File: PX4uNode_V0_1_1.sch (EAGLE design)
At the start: 129 parts, among them M3_MOUNT1101 MOUNT-HOLE3.1MM, M3_MOUNT1102 MOUNT-HOLE3.1MM, M3_MOUNT1103 MOUNT-HOLE3.1MM, M3_MOUNT1104 MOUNT-HOLE3.1MM, U101 STM32F4X7VX, U401 MAX3051, U402 MAX3051, X101 3.2x2.5 mm / 24 MHz / 15 ppm

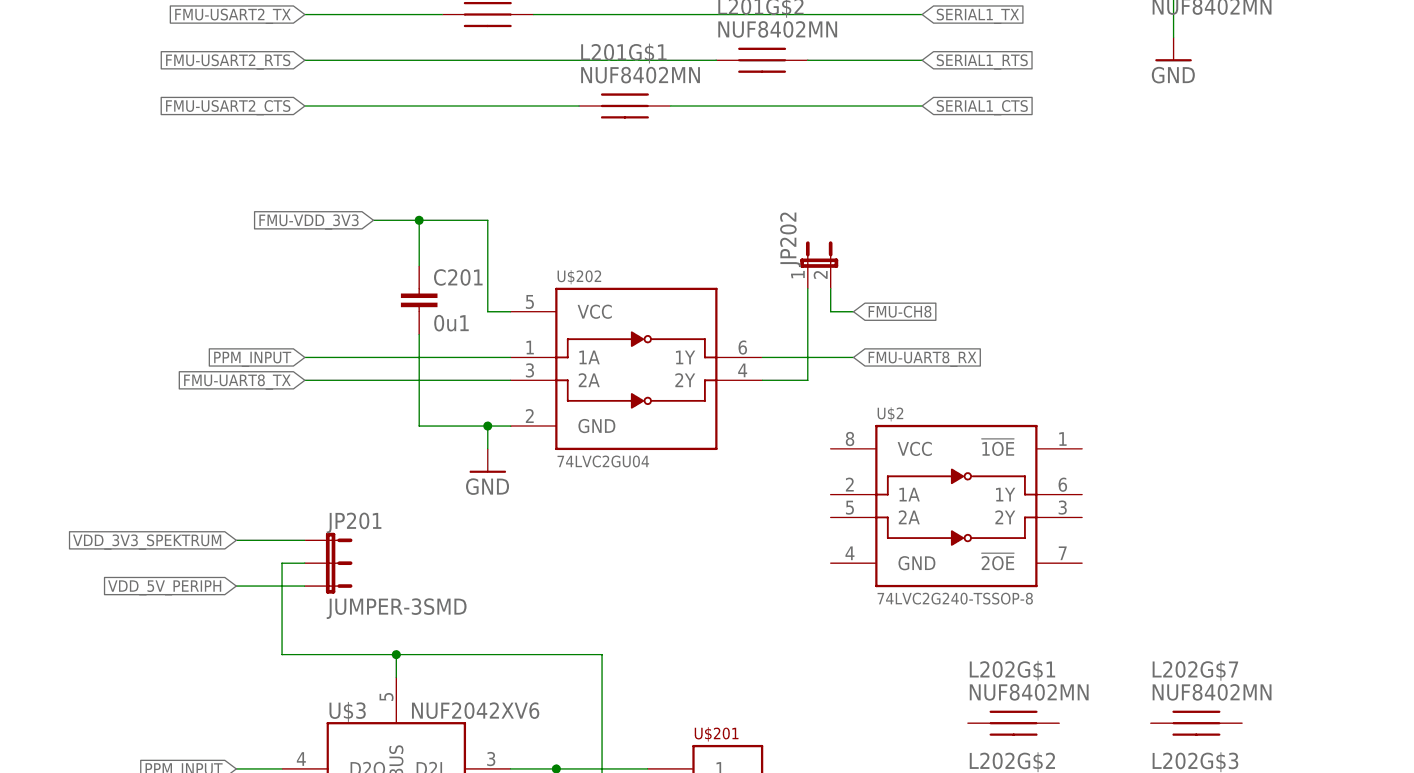
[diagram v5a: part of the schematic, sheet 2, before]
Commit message: Changed SBUS inverter for TSSOP part with output enable
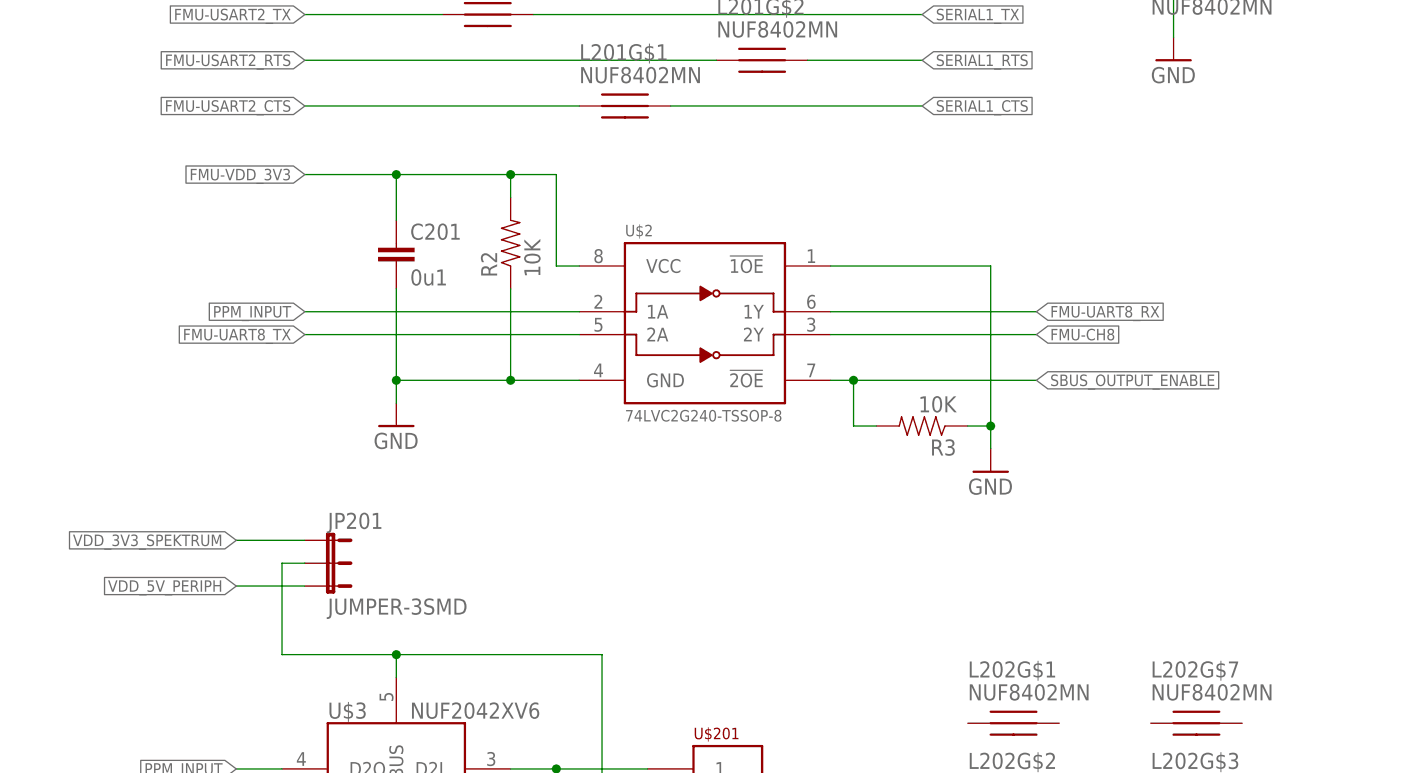
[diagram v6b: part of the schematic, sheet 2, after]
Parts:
- removed JP202: (no value), SparkFun-Passives:JUMPER-2SMD-NO
- removed U$202: 74LVC2GU04, pixhawk2:74LVC2GU04
- added R2, R3: 10K, pixhawk2:RESISTOR0402-RES
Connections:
- removed net !EX_VDD_5V_VALID: U101PORTB_L.PB5
- removed net N$5: JP202.1, U$202.2Y
- new net SBUS_OUTPUT_ENABLE: R3.2, U$2.!2OE, U101PORTB_L.PB5
- net FMU-CH8: now also U$2.2Y; no longer JP202.2
- net FMU-UART8_RX: now also U$2.1Y; no longer U$202.1Y
- net FMU-UART8_TX: now also U$2.2A; no longer U$202.2A
- net FMU-VDD_3V3: now also R2.2, U$2.VCC; no longer U$202.VCC
- net GND: now also R2.1, R3.1, U$2.!1OE, U$2.GND; no longer U$202.GND
- net PPM_INPUT: now also U$2.1A; no longer U$202.1A
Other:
- moved on the sheet: C201, U$2
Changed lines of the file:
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@@
 <attribute name="PARTNO" value="CC0402ZRY5V7BB104"/>
-</part>
-<part name="U$202" library="pixhawk2" deviceset="74LVC2GU04" device="">
-<attribute name="PARTNO" value="74LVC2GU04"/>
 </part>
 <part name="GND2" library="pixhawk2" deviceset="GND" device=""/>
@@
 <attribute name="BOM" value="EXCLUDE"/>
 <attribute name="PARTNO" value="*"/>
-</part>
-<part name="JP202" library="SparkFun-Passives" deviceset="JUMPER-2" device="SMD-NO">
-<attribute name="BOM" value="EXCLUDE"/>
 </part>
 <part name="JP1001" library="SparkFun-Connectors" deviceset="M01" device="SMD-4.5X1.5">
@@
 <part name="JP4" library="SparkFun-Connectors" deviceset="M01" device="PTH"/>
 <part name="U$2" library="pixhawk2" deviceset="74LVC2G240" device="-TSSOP-8"/>
+<part name="GND22" library="pixhawk2" deviceset="GND" device=""/>
+<part name="R2" library="pixhawk2" deviceset="RESISTOR" device="0402-RES" value="10K">
+<attribute name="PARTNO" value="RC0402FR-0710KL"/>
+</part>
+<part name="R3" library="pixhawk2" deviceset="RESISTOR" device="0402-RES" value="10K">
+<attribute name="PARTNO" value="RC0402FR-0710KL"/>
+</part>
 </parts>
 <sheets>
@@
 </segment>
 </net>
-<net name="!EX_VDD_5V_VALID" class="0">
+<net name="SBUS_OUTPUT_ENABLE" class="0">
 <segment>
 <pinref part="U101" gate="PORTB_L" pin="PB5"/>
-<wire x1="33.02" y1="96.52" x2="58.42" y2="96.52" width="0.1524" layer="91"/>
-<label x="58.42" y="96.52" size="1.27" layer="95" xref="yes"/>
+<wire x1="33.02" y1="96.52" x2="40.64" y2="96.52" width="0.1524" layer="91"/>
+<label x="40.64" y="96.52" size="1.27" layer="95" xref="yes"/>
 </segment>
 </net>
@@
 <instance part="L202" gate="G$7" x="147.32" y="60.96"/>
 <instance part="L202" gate="G$4" x="147.32" y="38.1"/>
-<instance part="U$202" gate="G$1" x="83.82" y="99.06">
-<attribute name="PARTNO" x="83.82" y="99.06" size="1.778" layer="96" display="off"/>
-</instance>
-<instance part="GND2" gate="1" x="68.58" y="88.9"/>
-<instance part="C201" gate="G$1" x="60.96" y="106.68">
-<attribute name="PARTNO" x="60.96" y="106.68" size="1.778" layer="96" display="off"/>
+<instance part="GND2" gate="1" x="58.42" y="93.98"/>
+<instance part="C201" gate="G$1" x="58.42" y="111.76" smashed="yes">
+<attribute name="PARTNO" x="58.42" y="111.76" size="1.778" layer="96" display="off"/>
+<attribute name="NAME" x="59.944" y="114.681" size="1.778" layer="95"/>
+<attribute name="VALUE" x="59.944" y="109.601" size="1.778" layer="96"/>
 </instance>
 <instance part="JP201" gate="G$1" x="50.8" y="81.28" rot="R270">
 <attribute name="BOM" x="50.8" y="81.28" size="1.778" layer="96" rot="R270" display="off"/>
-</instance>
-<instance part="JP202" gate="A" x="104.14" y="111.76">
-<attribute name="BOM" x="104.14" y="111.76" size="1.778" layer="96" display="off"/>
 </instance>
 <instance part="JP12" gate="G$1" x="220.98" y="147.32"/>
@@
 <instance part="GND19" gate="1" x="58.42" y="30.48"/>
 <instance part="U$3" gate="G$1" x="58.42" y="50.8"/>
-<instance part="U$2" gate="G$1" x="119.38" y="83.82"/>
+<instance part="U$2" gate="G$1" x="91.44" y="104.14"/>
+<instance part="GND22" gate="1" x="124.46" y="88.9"/>
+<instance part="R2" gate="G$1" x="71.12" y="114.3" rot="R90">
+<attribute name="PARTNO" x="71.12" y="114.3" size="1.778" layer="96" display="off"/>
+</instance>
+<instance part="R3" gate="G$1" x="116.84" y="93.98" rot="R180">
+<attribute name="PARTNO" x="116.84" y="93.98" size="1.778" layer="96" rot="R90" display="off"/>
+</instance>
 </instances>
 <busses>
@@
 <segment>
 <pinref part="GND2" gate="1" pin="GND"/>
-<wire x1="68.58" y1="91.44" x2="68.58" y2="93.98" width="0.1524" layer="91"/>
-<pinref part="U$202" gate="G$1" pin="GND"/>
-<wire x1="68.58" y1="93.98" x2="71.12" y2="93.98" width="0.1524" layer="91"/>
+<wire x1="58.42" y1="96.52" x2="58.42" y2="99.06" width="0.1524" layer="91"/>
+<wire x1="58.42" y1="99.06" x2="71.12" y2="99.06" width="0.1524" layer="91"/>
 <pinref part="C201" gate="G$1" pin="2"/>
-<wire x1="60.96" y1="104.14" x2="60.96" y2="93.98" width="0.1524" layer="91"/>
-<wire x1="60.96" y1="93.98" x2="68.58" y2="93.98" width="0.1524" layer="91"/>
-<junction x="68.58" y="93.98"/>
+<wire x1="71.12" y1="99.06" x2="78.74" y2="99.06" width="0.1524" layer="91"/>
+<wire x1="58.42" y1="109.22" x2="58.42" y2="99.06" width="0.1524" layer="91"/>
+<junction x="58.42" y="99.06"/>
+<pinref part="U$2" gate="G$1" pin="GND"/>
+<pinref part="R2" gate="G$1" pin="1"/>
+<wire x1="71.12" y1="109.22" x2="71.12" y2="99.06" width="0.1524" layer="91"/>
+<junction x="71.12" y="99.06"/>
 </segment>
 <segment>
@@
 <pinref part="U$3" gate="G$1" pin="GND"/>
 <wire x1="58.42" y1="33.02" x2="58.42" y2="35.56" width="0.1524" layer="91"/>
+</segment>
+<segment>
+<pinref part="GND22" gate="1" pin="GND"/>
+<wire x1="124.46" y1="91.44" x2="124.46" y2="93.98" width="0.1524" layer="91"/>
+<pinref part="U$2" gate="G$1" pin="!1OE"/>
+<wire x1="124.46" y1="93.98" x2="124.46" y2="111.76" width="0.1524" layer="91"/>
+<wire x1="124.46" y1="111.76" x2="106.68" y2="111.76" width="0.1524" layer="91"/>
+<pinref part="R3" gate="G$1" pin="1"/>
+<wire x1="121.92" y1="93.98" x2="124.46" y2="93.98" width="0.1524" layer="91"/>
+<junction x="124.46" y="93.98"/>
 </segment>
 </net>
@@
 </segment>
 <segment>
-<label x="48.26" y="101.6" size="1.27" layer="95" rot="R180" xref="yes"/>
-<pinref part="U$202" gate="G$1" pin="1A"/>
-<wire x1="48.26" y1="101.6" x2="71.12" y2="101.6" width="0.1524" layer="91"/>
+<label x="48.26" y="106.68" size="1.27" layer="95" rot="R180" xref="yes"/>
+<wire x1="48.26" y1="106.68" x2="78.74" y2="106.68" width="0.1524" layer="91"/>
+<pinref part="U$2" gate="G$1" pin="1A"/>
 </segment>
 </net>
@@
 </segment>
 </net>
-<net name="FMU-VDD_3V3" class="1">
-<segment>
-<wire x1="71.12" y1="106.68" x2="68.58" y2="106.68" width="0.1524" layer="91"/>
-<wire x1="68.58" y1="106.68" x2="68.58" y2="116.84" width="0.1524" layer="91"/>
-<wire x1="68.58" y1="116.84" x2="60.96" y2="116.84" width="0.1524" layer="91"/>
-<label x="55.88" y="116.84" size="1.27" layer="95" rot="R180" xref="yes"/>
-<pinref part="U$202" gate="G$1" pin="VCC"/>
-<pinref part="C201" gate="G$1" pin="1"/>
-<wire x1="60.96" y1="116.84" x2="55.88" y2="116.84" width="0.1524" layer="91"/>
-<wire x1="60.96" y1="111.76" x2="60.96" y2="116.84" width="0.1524" layer="91"/>
-<junction x="60.96" y="116.84"/>
-</segment>
-</net>
 <net name="FMU-UART8_RX" class="0">
 <segment>
-<pinref part="U$202" gate="G$1" pin="1Y"/>
-<wire x1="99.06" y1="101.6" x2="109.22" y2="101.6" width="0.1524" layer="91"/>
-<label x="109.22" y="101.6" size="1.27" layer="95" xref="yes"/>
+<wire x1="106.68" y1="106.68" x2="129.54" y2="106.68" width="0.1524" layer="91"/>
+<label x="129.54" y="106.68" size="1.27" layer="95" xref="yes"/>
+<pinref part="U$2" gate="G$1" pin="1Y"/>
 </segment>
 </net>
 <net name="FMU-UART8_TX" class="0">
 <segment>
-<wire x1="71.12" y1="99.06" x2="48.26" y2="99.06" width="0.1524" layer="91"/>
-<label x="48.26" y="99.06" size="1.27" layer="95" rot="MR0" xref="yes"/>
-<pinref part="U$202" gate="G$1" pin="2A"/>
-</segment>
-</net>
-<net name="N$5" class="0">
-<segment>
-<pinref part="U$202" gate="G$1" pin="2Y"/>
-<wire x1="99.06" y1="99.06" x2="104.14" y2="99.06" width="0.1524" layer="91"/>
-<pinref part="JP202" gate="A" pin="1"/>
-<wire x1="104.14" y1="109.22" x2="104.14" y2="99.06" width="0.1524" layer="91"/>
+<wire x1="78.74" y1="104.14" x2="48.26" y2="104.14" width="0.1524" layer="91"/>
+<label x="48.26" y="104.14" size="1.27" layer="95" rot="MR0" xref="yes"/>
+<pinref part="U$2" gate="G$1" pin="2A"/>
 </segment>
 </net>
 <net name="FMU-CH8" class="0">
 <segment>
-<wire x1="106.68" y1="106.68" x2="109.22" y2="106.68" width="0.1524" layer="91"/>
-<pinref part="JP202" gate="A" pin="2"/>
-<wire x1="106.68" y1="106.68" x2="106.68" y2="109.22" width="0.1524" layer="91"/>
-<label x="109.22" y="106.68" size="1.27" layer="95" xref="yes"/>
+<label x="129.54" y="104.14" size="1.27" layer="95" xref="yes"/>
+<wire x1="106.68" y1="104.14" x2="129.54" y2="104.14" width="0.1524" layer="91"/>
+<pinref part="U$2" gate="G$1" pin="2Y"/>
 </segment>
 </net>
@@
 </segment>
 </net>
+<net name="FMU-VDD_3V3" class="1">
+<segment>
+<label x="48.26" y="121.92" size="1.27" layer="95" rot="R180" xref="yes"/>
+<wire x1="48.26" y1="121.92" x2="58.42" y2="121.92" width="0.1524" layer="91"/>
+<pinref part="U$2" gate="G$1" pin="VCC"/>
+<wire x1="58.42" y1="121.92" x2="71.12" y2="121.92" width="0.1524" layer="91"/>
+<wire x1="71.12" y1="121.92" x2="76.2" y2="121.92" width="0.1524" layer="91"/>
+<wire x1="78.74" y1="111.76" x2="76.2" y2="111.76" width="0.1524" layer="91"/>
+<wire x1="76.2" y1="111.76" x2="76.2" y2="121.92" width="0.1524" layer="91"/>
+<pinref part="C201" gate="G$1" pin="1"/>
+<wire x1="58.42" y1="116.84" x2="58.42" y2="121.92" width="0.1524" layer="91"/>
+<pinref part="R2" gate="G$1" pin="2"/>
+<wire x1="71.12" y1="119.38" x2="71.12" y2="121.92" width="0.1524" layer="91"/>
+<junction x="58.42" y="121.92"/>
+<junction x="71.12" y="121.92"/>
+</segment>
+</net>
+<net name="SBUS_OUTPUT_ENABLE" class="0">
+<segment>
+<pinref part="U$2" gate="G$1" pin="!2OE"/>
+<wire x1="106.68" y1="99.06" x2="109.22" y2="99.06" width="0.1524" layer="91"/>
+<label x="129.54" y="99.06" size="1.27" layer="95" xref="yes"/>
+<pinref part="R3" gate="G$1" pin="2"/>
+<wire x1="109.22" y1="99.06" x2="129.54" y2="99.06" width="0.1524" layer="91"/>
+<wire x1="111.76" y1="93.98" x2="109.22" y2="93.98" width="0.1524" layer="91"/>
+<wire x1="109.22" y1="93.98" x2="109.22" y2="99.06" width="0.1524" layer="91"/>
+<junction x="109.22" y="99.06"/>
+</segment>
+</net>

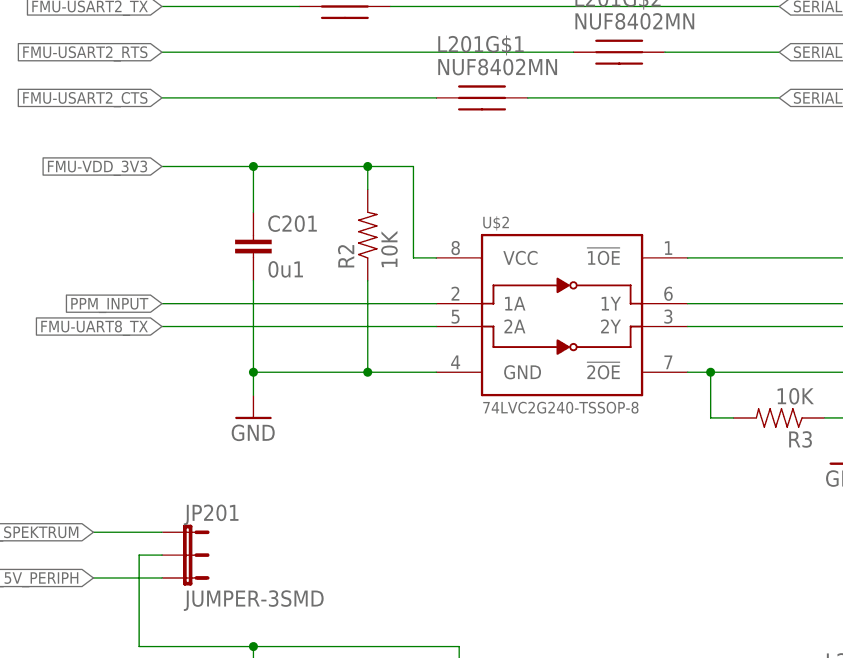
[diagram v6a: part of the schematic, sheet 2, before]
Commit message: SBUS inverter changed to VSSOP and layout done
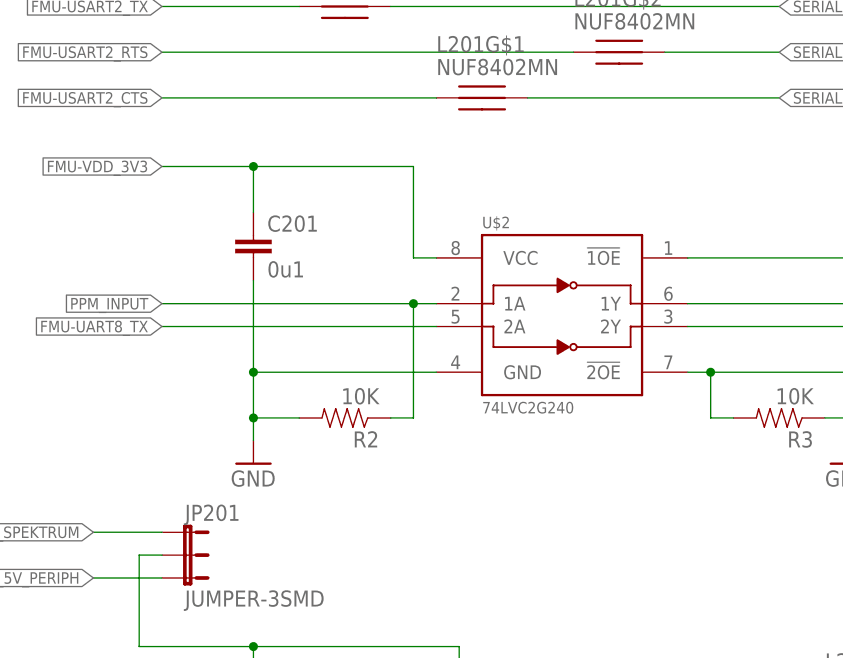
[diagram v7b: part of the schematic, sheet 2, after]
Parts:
- U$2: value 74LVC2G240-TSSOP-8 -> 74LVC2G240; device pixhawk2:74LVC2G240-TSSOP-8 -> PX4lite:74LVC2G240
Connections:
- net FMU-VDD_3V3: no longer R2.2
- net GND: now also R2.2; no longer R2.1
- net PPM_INPUT: now also R2.1
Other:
- moved on the sheet: R2
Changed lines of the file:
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@@
 <part name="JP3" library="SparkFun-Connectors" deviceset="M01" device="PTH"/>
 <part name="JP4" library="SparkFun-Connectors" deviceset="M01" device="PTH"/>
-<part name="U$2" library="pixhawk2" deviceset="74LVC2G240" device="-TSSOP-8"/>
+<part name="U$2" library="PX4lite" deviceset="74LVC2G240" device=""/>
 <part name="GND22" library="pixhawk2" deviceset="GND" device=""/>
 <part name="R2" library="pixhawk2" deviceset="RESISTOR" device="0402-RES" value="10K">
@@
 <instance part="L202" gate="G$7" x="147.32" y="60.96"/>
 <instance part="L202" gate="G$4" x="147.32" y="38.1"/>
-<instance part="GND2" gate="1" x="58.42" y="93.98"/>
+<instance part="GND2" gate="1" x="58.42" y="88.9"/>
 <instance part="C201" gate="G$1" x="58.42" y="111.76" smashed="yes">
 <attribute name="PARTNO" x="58.42" y="111.76" size="1.778" layer="96" display="off"/>
@@
 <instance part="U$2" gate="G$1" x="91.44" y="104.14"/>
 <instance part="GND22" gate="1" x="124.46" y="88.9"/>
-<instance part="R2" gate="G$1" x="71.12" y="114.3" rot="R90">
-<attribute name="PARTNO" x="71.12" y="114.3" size="1.778" layer="96" display="off"/>
+<instance part="R2" gate="G$1" x="68.58" y="93.98" rot="R180">
+<attribute name="PARTNO" x="68.58" y="93.98" size="1.778" layer="96" rot="R90" display="off"/>
 </instance>
 <instance part="R3" gate="G$1" x="116.84" y="93.98" rot="R180">
@@
 <segment>
 <pinref part="GND2" gate="1" pin="GND"/>
-<wire x1="58.42" y1="96.52" x2="58.42" y2="99.06" width="0.1524" layer="91"/>
-<wire x1="58.42" y1="99.06" x2="71.12" y2="99.06" width="0.1524" layer="91"/>
+<wire x1="58.42" y1="91.44" x2="58.42" y2="93.98" width="0.1524" layer="91"/>
+<wire x1="58.42" y1="93.98" x2="58.42" y2="99.06" width="0.1524" layer="91"/>
+<wire x1="58.42" y1="99.06" x2="78.74" y2="99.06" width="0.1524" layer="91"/>
 <pinref part="C201" gate="G$1" pin="2"/>
-<wire x1="71.12" y1="99.06" x2="78.74" y2="99.06" width="0.1524" layer="91"/>
 <wire x1="58.42" y1="109.22" x2="58.42" y2="99.06" width="0.1524" layer="91"/>
 <junction x="58.42" y="99.06"/>
 <pinref part="U$2" gate="G$1" pin="GND"/>
-<pinref part="R2" gate="G$1" pin="1"/>
-<wire x1="71.12" y1="109.22" x2="71.12" y2="99.06" width="0.1524" layer="91"/>
-<junction x="71.12" y="99.06"/>
+<pinref part="R2" gate="G$1" pin="2"/>
+<wire x1="63.5" y1="93.98" x2="58.42" y2="93.98" width="0.1524" layer="91"/>
+<junction x="58.42" y="93.98"/>
 </segment>
 <segment>
@@
 <segment>
 <label x="48.26" y="106.68" size="1.27" layer="95" rot="R180" xref="yes"/>
-<wire x1="48.26" y1="106.68" x2="78.74" y2="106.68" width="0.1524" layer="91"/>
+<wire x1="48.26" y1="106.68" x2="76.2" y2="106.68" width="0.1524" layer="91"/>
 <pinref part="U$2" gate="G$1" pin="1A"/>
+<pinref part="R2" gate="G$1" pin="1"/>
+<wire x1="76.2" y1="106.68" x2="78.74" y2="106.68" width="0.1524" layer="91"/>
+<wire x1="73.66" y1="93.98" x2="76.2" y2="93.98" width="0.1524" layer="91"/>
+<wire x1="76.2" y1="93.98" x2="76.2" y2="106.68" width="0.1524" layer="91"/>
+<junction x="76.2" y="106.68"/>
 </segment>
 </net>
@@
 <wire x1="48.26" y1="121.92" x2="58.42" y2="121.92" width="0.1524" layer="91"/>
 <pinref part="U$2" gate="G$1" pin="VCC"/>
-<wire x1="58.42" y1="121.92" x2="71.12" y2="121.92" width="0.1524" layer="91"/>
-<wire x1="71.12" y1="121.92" x2="76.2" y2="121.92" width="0.1524" layer="91"/>
+<wire x1="58.42" y1="121.92" x2="76.2" y2="121.92" width="0.1524" layer="91"/>
 <wire x1="78.74" y1="111.76" x2="76.2" y2="111.76" width="0.1524" layer="91"/>
 <wire x1="76.2" y1="111.76" x2="76.2" y2="121.92" width="0.1524" layer="91"/>
 <pinref part="C201" gate="G$1" pin="1"/>
 <wire x1="58.42" y1="116.84" x2="58.42" y2="121.92" width="0.1524" layer="91"/>
-<pinref part="R2" gate="G$1" pin="2"/>
-<wire x1="71.12" y1="119.38" x2="71.12" y2="121.92" width="0.1524" layer="91"/>
 <junction x="58.42" y="121.92"/>
-<junction x="71.12" y="121.92"/>
-</segment>
-</net>
+</segment>
+</net>
